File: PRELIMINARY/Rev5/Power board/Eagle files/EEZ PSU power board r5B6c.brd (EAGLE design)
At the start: 74 x 135 mm, 248 parts, among them IC1 LTC3864, IC10 MCP23S08-E/SO, IC11 DAC8552, IC12 REF5025, IC13 ADS1120, IC14 ADG465SOT-23, IC15 TS5A9411DCKT, IC16 LP339D, IC2 Si8610BC-B-IS, IC3 MC79L05, IC4 MC78L05, IC5 LM5574, IC6 LP2951SO8, IC7 TL072D, IC8 TL072D, IC9 OP27GSZ, Q1 SUD19P06-60, Q10 MMBT5401, Q11 MMBT5401, Q12 MMBT5551, Q13 MMBT5551, Q14 BSS84P, Q15 2N7002, Q2 MMBT5401, Q3 2N7002, Q4 IRFP250N, Q5 BC857C, Q6 BC846C, Q7 BCP56-16.115, Q8 IRFR5410, Q9 BCP56-16.115, X1 282836-2, X2 826925-3, X3 SSW-102-02-S-S, X4 SSW-113-02-T-D-RA, X5 TSW-104-08-L-D

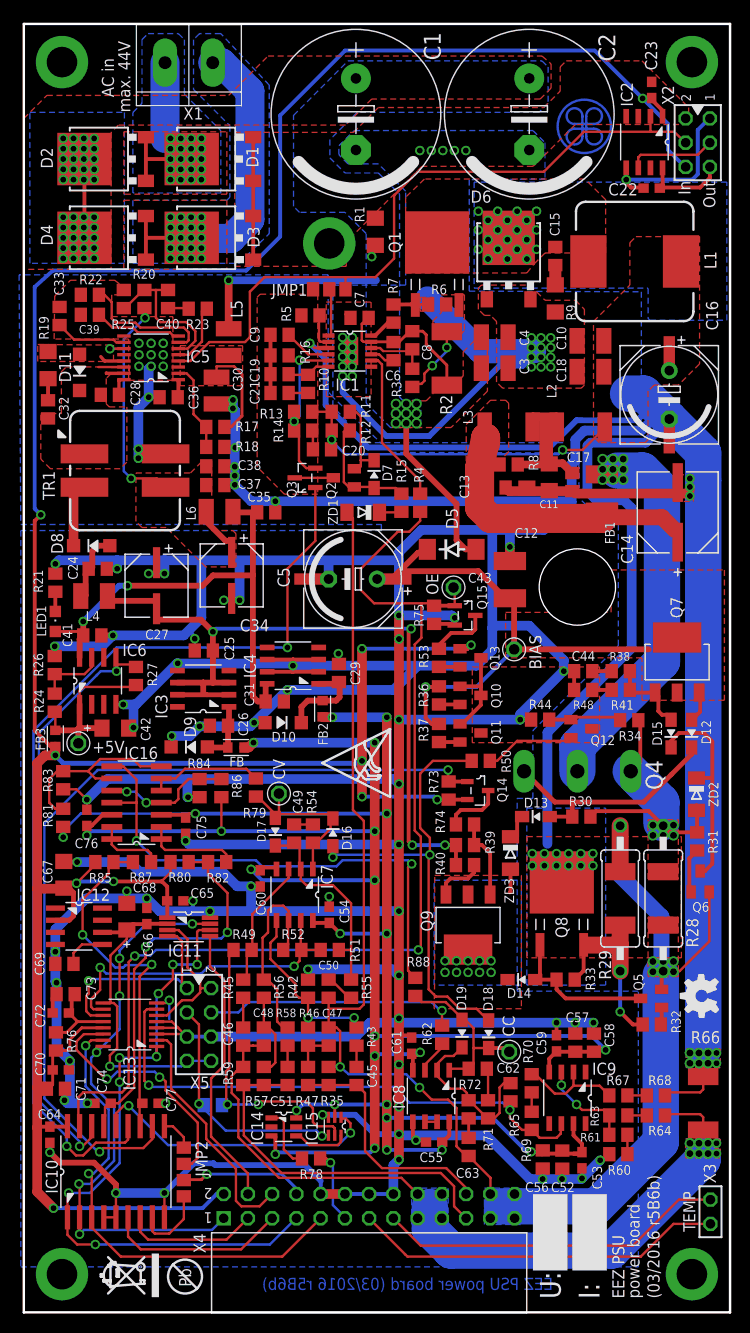
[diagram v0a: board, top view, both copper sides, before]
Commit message: Pads for DC input added into EEZ PSU power board r5B6c
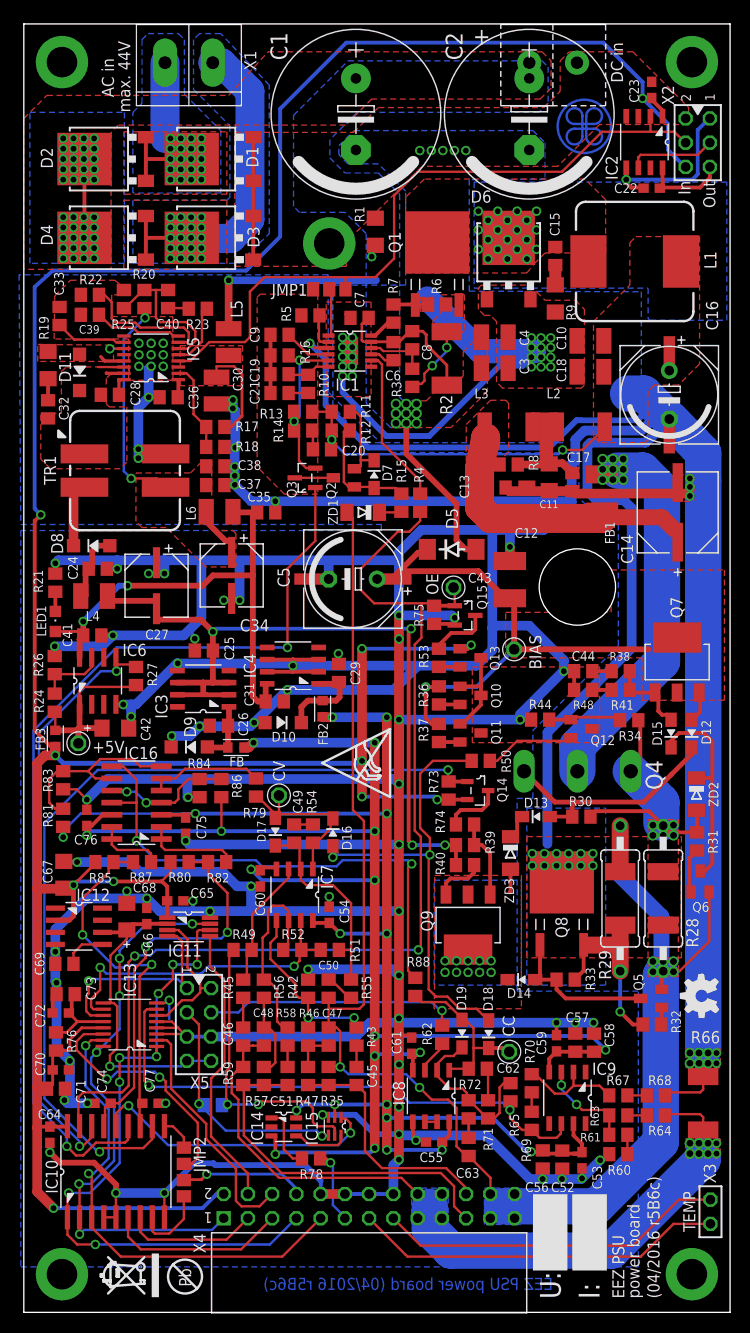
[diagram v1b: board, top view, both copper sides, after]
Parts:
- SH1, SH2: device EEZ_Lib1:SHORT -> EEZ_Lib1:SHORT_NOHOLE
- moved CV 0.19 mm to (26.7, 54.2)
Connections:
- net GND: now also SH1.P$2, SH2.P$2; no longer SH1.2, SH2.2
- net POUT-: now also SH1.P$1; no longer SH1.1
- net SGND: now also SH2.P$1; no longer SH2.1
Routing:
- net +5V: track 331.3 -> 334.1 mm
- net GND: track 855.3 -> 853.8 mm, vias 122 -> 123
- net DC_OUT: vias 51 -> 52
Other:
- board text added: "(04/2016 r5B6c)"
- board text added: "+"
- board text added: "DC in"
- board text added: "EEZ PSU power board (04/2016 r5B6c)"
- board text removed: "(03/2016 r5B6b)"
- board text removed: "EEZ PSU power board (03/2016 r5B6b)"
